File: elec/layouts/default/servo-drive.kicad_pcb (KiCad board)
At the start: 4 copper layers, 37.6 x 39.9 mm, 136 parts, among them U37 8Mhz

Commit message: Something fishy is going on with interfaces
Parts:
- removed U30: , lib:LED0603-RD
- added R40: , Resistor_SMD:R_0402_1005Metric, F.Cu at (179.8, 92.0)
- J1, R19, R20, U13, U2, U37: moved to B.Cu
- R39: value 1k -> (none)
- U26, U27: moved to F.Cu
- moved U2 66.5 mm to (222.4, 113.4), turned to 180 degrees
- moved J1 51.2 mm to (210.9, 115.7), turned to 180 degrees
- moved U25 50.9 mm to (229.0, 113.8), turned to -90 degrees
- moved U15 46.8 mm to (211.0, 118.7)
- moved R20 26.5 mm to (209.2, 111.4)
- moved R39 25.8 mm to (213.8, 92.7), turned to 180 degrees
- moved R24 25.0 mm to (213.9, 88.4), turned to 180 degrees
- moved U29 22.9 mm to (213.3, 89.6)
- moved R19 20.3 mm to (212.2, 111.3)
- moved U13 19.8 mm to (213.6, 89.9), turned to 45 degrees
- moved C1 19.8 mm to (197.6, 99.1)
- moved C19 19.8 mm to (197.6, 98.1)
- moved U37 17.4 mm to (208.9, 84.7), turned to -135 degrees
- moved U38 10.1 mm to (217.5, 114.4), turned to -90 degrees
- moved U23 9.04 mm to (222.3, 113.3)
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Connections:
- net SpinServoNEMA17-data_out renamed SpinServoNEMA17-data_in
- net SpinServoNEMA17-phase_b renamed SpinServoNEMA17-INLB
- net SpinServoNEMA17-phase_c renamed SpinServoNEMA17-INLC
- net _a-i_in-1 renamed _a-i_in-2
- net _b-i_in-1 renamed _b-i_in-2
- net _c-i_in-1 renamed _c-i_in-2
- net _i_sense-in-4 renamed _i_sense-gnd-7
- net _i_sense-in_n-6 renamed _i_sense-in_n
- net _i_sense-in_n-7 renamed _i_sense-in_n-1
- net _i_sense-in_n-8 renamed _i_sense-output-17
- net _i_sense-in_p-1 renamed _i_sense-output-15
- net _i_sense-in_p-2 renamed _i_sense-output-16
- net _i_sense-input-9 renamed _i_sense-p1-4
- net _i_sense-out-3 renamed _i_sense-in
- net _i_sense-out-4 renamed _i_sense-gnd-6
- net _i_sense-output-7 renamed _i_sense-output-14
- net ldo_3v3-adj-1 renamed ldo_3v3-adj
- net ldo_5v-output renamed ldo_5v-adj-1
- net micro-input-2 renamed micro-PF1_OSC_OUT-1
- C1 pad 1: SpinServoNEMA17-vcc -> SpinServoNEMA17-input
- C13 pad 1: SpinServoNEMA17-vcc -> SpinServoNEMA17-input
- C14 pad 1: SpinServoNEMA17-vcc -> SpinServoNEMA17-input
- C15 pad 1: SpinServoNEMA17-vcc -> SpinServoNEMA17-input
- C17 pad 1: SpinServoNEMA17-vcc -> SpinServoNEMA17-input
- C19 pad 1: SpinServoNEMA17-vcc -> SpinServoNEMA17-input
- C28 pad 1: SpinServoNEMA17-vcc-1 -> SpinServoNEMA17-in
- C40 pad 1: SpinServoNEMA17-vcc -> SpinServoNEMA17-input
- C41 pad 1: power_stage-bs-4 -> power_stage-bs-3
- C42 pad 1: micro-PF0_OSC_IN -> micro-in-1
- C43 pad 1: power_stage-bs-3 -> power_stage-bs-2
- C45 pad 1: power_stage-bs-2 -> power_stage-bs-1
- C46 pad 1: SpinServoNEMA17-vcc -> SpinServoNEMA17-gnd
- C46 pad 2: SpinServoNEMA17-gnd -> SpinServoNEMA17-input
- C7 pad 1: canbus-v_3_3-2 -> SpinServoNEMA17-input
- C7 pad 2: canbus-gnd-2 -> SpinServoNEMA17-gnd
- C9 pad 2: canbus-gnd-2 -> SpinServoNEMA17-gnd
- J1 pad 1: SpinServoNEMA17-gnd -> usbc-gnd
- J1 pad 2: SpinServoNEMA17-gnd -> usbc-gnd
- J1 pad 3: SpinServoNEMA17-gnd -> usbc-gnd
- J1 pad 4: SpinServoNEMA17-gnd -> usbc-gnd
- J1 pad A1: SpinServoNEMA17-gnd -> usbc-gnd
- J1 pad A12: SpinServoNEMA17-gnd -> usbc-gnd
- J1 pad A7: SpinServoNEMA17-gnd -> SpinServoNEMA17-dm
- J1 pad B1: SpinServoNEMA17-gnd -> usbc-gnd
- J1 pad B12: SpinServoNEMA17-gnd -> usbc-gnd
- J1 pad B7: SpinServoNEMA17-gnd -> SpinServoNEMA17-dm
- R1 pad 1: SpinServoNEMA17-vcc -> SpinServoNEMA17-input
- R10 pad 1: SpinServoNEMA17-dp -> micro-PA11-1
- R10 pad 2: SpinServoNEMA17-dp -> SpinServoNEMA17-dm
- R11 pad 1: SpinServoNEMA17-gnd -> micro-PA12-1
- R11 pad 2: SpinServoNEMA17-vcc -> SpinServoNEMA17-input
- R15 pad 1: SpinServoNEMA17-p3 -> SpinServoNEMA17-p2
- R2 pad 1: SpinServoNEMA17-vcc -> SpinServoNEMA17-input
- R21 pad 1: SpinServoNEMA17-vcc -> SpinServoNEMA17-input
- R23 pad 1: SpinServoNEMA17-p2 -> SpinServoNEMA17-p3
- R27 pad 1: SpinServoNEMA17-vcc-1 -> SpinServoNEMA17-in
- R3 pad 2: SpinServoNEMA17-in -> SpinServoNEMA17-in-1
- R39 pad 1: debug_led_2-A-2 -> SpinServoNEMA17-sda
- R39 pad 2: SpinServoNEMA17-gnd -> SpinServoNEMA17-input
- R9 pad 1: SpinServoNEMA17-gnd -> micro-PA12-1
- R9 pad 2: SpinServoNEMA17-gnd -> SpinServoNEMA17-dp
- U11 pad 1: SpinServoNEMA17-in -> SpinServoNEMA17-in-1
- U11 pad 2: SpinServoNEMA17-vcc -> SpinServoNEMA17-input
- U12 pad 14: power_stage-bs-2 -> power_stage-bs-1
- U12 pad 17: power_stage-bs-3 -> power_stage-bs-2
- U12 pad 20: power_stage-bs-4 -> power_stage-bs-3
- U12 pad 5: SpinServoNEMA17-vcc -> SpinServoNEMA17-input
- U13 pad 13: SpinServoNEMA17-in -> SpinServoNEMA17-in-1
- U13 pad 15: micro-PA7-2 -> SpinServoNEMA17-led_pixel
- U13 pad 20: SpinServoNEMA17-vcc -> SpinServoNEMA17-input
- U13 pad 21: SpinServoNEMA17-vcc -> SpinServoNEMA17-input
- U13 pad 22: micro-PB10-2 -> micro-tdo
- U13 pad 23: SpinServoNEMA17-vcc -> SpinServoNEMA17-input
- U13 pad 24: micro-PB11-2 -> SpinServoNEMA17-cs
- U13 pad 25: SpinServoNEMA17-cs -> SpinServoNEMA17-vin_sense
- U13 pad 30: SpinServoNEMA17-vin_sense -> micro-PA8-2
- U13 pad 33: SpinServoNEMA17-dp -> micro-PA11-1
- U13 pad 34: SpinServoNEMA17-gnd -> micro-PA12-1
- U13 pad 35: SpinServoNEMA17-vcc -> SpinServoNEMA17-input
- U13 pad 36: micro-tms -> micro-tms-1
- U13 pad 37: micro-tck-1 -> micro-tck-2
- U13 pad 38: micro-PA15 -> micro-tdi-1
- U13 pad 41: micro-PB3 -> micro-PB3-2
- U13 pad 42: micro-rst -> micro-PB4-1
- U13 pad 43: SpinServoNEMA17-led_pixel -> micro-PB5-1
- U13 pad 44: micro-PB6-2 -> micro-PB6-1
- U13 pad 46: SpinServoNEMA17-sda -> SpinServoNEMA17-scl
- U13 pad 47: SpinServoNEMA17-gnd -> SpinServoNEMA17-sda
- U13 pad 48: SpinServoNEMA17-vcc -> SpinServoNEMA17-input
- U13 pad 5: micro-PF0_OSC_IN -> micro-in-1
- U14 pad 2: SpinServoNEMA17-vcc-1 -> SpinServoNEMA17-in
- U15 pad 2: SpinServoNEMA17-vcc -> SpinServoNEMA17-input
- U15 pad 4: SpinServoNEMA17-gnd -> SpinServoNEMA17-scl
- U16 pad 1: SpinServoNEMA17-vcc -> SpinServoNEMA17-input
- U16 pad 10: micro-rst -> micro-tdo
- U16 pad 2: micro-tms -> micro-tck-2
- U16 pad 4: micro-tck-1 -> micro-vcc
- U16 pad 6: micro-PB3 -> micro-tdi-1
- U16 pad 8: micro-PA15 -> micro-tms-1
- U18 pad 10: SpinServoNEMA17-gnd -> SpinServoNEMA17-input
- U18 pad 13: SpinServoNEMA17-vcc -> SpinServoNEMA17-gnd
- U18 pad 17: SpinServoNEMA17-gnd -> SpinServoNEMA17-input
- U18 pad 8: SpinServoNEMA17-gnd -> SpinServoNEMA17-input
- U2 pad 1: xt30_2-gnd-1 -> SpinServoNEMA17-gnd
- U2 pad 2: xt30_2-vin-1 -> SpinServoNEMA17-in
- U20 pad 5: SpinServoNEMA17-vcc -> SpinServoNEMA17-input
- U21 pad 5: SpinServoNEMA17-vcc -> SpinServoNEMA17-input
- U23 pad 5: SpinServoNEMA17-vcc -> SpinServoNEMA17-input
- U24 pad 5: SpinServoNEMA17-vcc -> SpinServoNEMA17-input
- U25 pad 1: SpinServoNEMA17-gnd -> micro-PB6-1
- U25 pad 2: canbus-gnd-2 -> SpinServoNEMA17-gnd
- U25 pad 3: canbus-v_3_3-2 -> SpinServoNEMA17-input
- U25 pad 4: SpinServoNEMA17-dp -> micro-PB5-1
- U25 pad 6: SpinServoNEMA17-p2 -> SpinServoNEMA17-p3
- U25 pad 7: SpinServoNEMA17-p3 -> SpinServoNEMA17-p2
- U25 pad 8: canbus-gnd-2 -> SpinServoNEMA17-gnd
- U26 pad 1: SpinServoNEMA17-gnd -> SpinServoNEMA17-input
- U27 pad 1: SpinServoNEMA17-gnd -> SpinServoNEMA17-input
- U29 pad 1: micro-PF0_OSC_IN -> micro-PB4-1
- U37 pad 1: micro-PF0_OSC_IN -> micro-in-1
- U4 pad 5: SpinServoNEMA17-vcc -> SpinServoNEMA17-input
- U6 pad 4: SpinServoNEMA17-vcc-1 -> SpinServoNEMA17-in
- U6 pad 5: SpinServoNEMA17-vcc-1 -> SpinServoNEMA17-in
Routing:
- net (no net): track 153.2 -> 54.9 mm, vias 12 -> 2
- net SpinServoNEMA17-p2: track 0.00 -> 28.0 mm, vias 0 -> 4
- net SpinServoNEMA17-c_isense: track 27.3 -> 0.04 mm, vias 2 -> 0
- net SpinServoNEMA17-INLB: track 32.6 -> 6.98 mm, vias 4 -> 3
- net SpinServoNEMA17-in: track 17.5 -> 0.00 mm, vias 2 -> 0
- net SpinServoNEMA17-phase_a: track 34.3 -> 17.3 mm, vias 4 -> 3
- net SpinServoNEMA17-a_isense: track 17.7 -> 1.12 mm, vias 2 -> 1
- net SpinServoNEMA17-in-1: track 0.00 -> 16.2 mm, vias 0 -> 1
- net micro-tdi-1: track 0.00 -> 15.0 mm, vias 0 -> 2
- net micro-tck-1: track 11.8 -> 0.00 mm, vias 1 -> 0
- net micro-tms-1: track 0.00 -> 10.3 mm, vias 0 -> 1
- net micro-tms: track 10.3 -> 0.00 mm, vias 1 -> 0
- net micro-PB3: track 9.85 -> 0.00 mm, vias 1 -> 0
- net SpinServoNEMA17-vcc: track 8.80 -> 0.00 mm, vias 6 -> 0
- net SpinServoNEMA17-data_in: track 7.35 -> 0.00 mm
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- removed copper zone on F.Cu, net SpinServoNEMA17-vcc-1
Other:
- board text removed: "BOOT0"
- board text removed: "RESET"

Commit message: layout complete
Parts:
- removed U38: , lib:SOD-323_L1.8-W1.3-LS2.5-RD
- added U30: , lib:SOD-323_L1.8-W1.3-LS2.5-RD, F.Cu at (217.6, 114.3)
- C13, C14, C15, C17, C40, C42, C44, R10, R11, R7, R9: moved to B.Cu
- moved R15 55.4 mm to (237.2, 113.7)
- moved R23 55.0 mm to (237.2, 114.7)
- moved C9 53.4 mm to (237.2, 112.8), turned to 180 degrees
- moved R40 41.9 mm to (213.6, 116.7), turned to -90 degrees
- moved C17 40.5 mm to (219.0, 86.7), turned to 45 degrees
- moved C14 40.4 mm to (214.4, 96.5), turned to -45 degrees
- moved C13 40.0 mm to (217.6, 85.2), turned to 45 degrees
- moved C15 39.8 mm to (215.1, 95.8), turned to -45 degrees
- moved C40 39.6 mm to (218.3, 85.9), turned to 45 degrees
- moved R9 35.7 mm to (210.1, 111.3), turned to -90 degrees
- moved R10 34.6 mm to (211.2, 111.3), turned to -90 degrees
- moved C44 31.9 mm to (210.5, 83.2), turned to 135 degrees
- moved R11 28.1 mm to (216.8, 95.4), turned to -90 degrees
- moved C42 28.0 mm to (206.8, 83.5), turned to 45 degrees
- moved C7 27.2 mm to (210.7, 108.0), turned to 90 degrees
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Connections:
- net SpinServoNEMA17-INLB renamed SpinServoNEMA17-INHB
- net SpinServoNEMA17-INLC renamed SpinServoNEMA17-INHC
- net SpinServoNEMA17-phase_a renamed SpinServoNEMA17-PA0
- net SpinServoNEMA17-vbus renamed usbc-vbus-1
- net SpinServoNEMA17-vin_sense renamed SpinServoNEMA17-out-1
- net _a-i_in-2 renamed _a-gnd
- net _b-i_in-2 renamed _b-i_in-1
- net _c-i_in-2 renamed _c-i_in
- net _i_sense-gnd-6 renamed _i_sense-gnd
- net _i_sense-gnd-7 renamed _i_sense-out-1
- net _i_sense-in renamed _i_sense-in-6
- net _i_sense-in_n renamed _i_sense-in_n-7
- net _i_sense-in_n-1 renamed _i_sense-output-6
- net _i_sense-input-14 renamed _i_sense-p1-6
- net _i_sense-output-14 renamed _i_sense-output-4
- net _i_sense-output-15 renamed _i_sense-output-5
- net _i_sense-output-16 renamed _i_sense-output-7
- net _i_sense-output-17 renamed _i_sense-in_n-8
- net micro-PB5-1 renamed micro-can_rx
- net micro-PB6-1 renamed micro-can_tx
- net micro-in-1 renamed micro-PF0_OSC_IN
- C1 pad 1: SpinServoNEMA17-input -> SpinServoNEMA17-out
- C13 pad 1: SpinServoNEMA17-input -> SpinServoNEMA17-out
- C14 pad 1: SpinServoNEMA17-input -> SpinServoNEMA17-out
- C15 pad 1: SpinServoNEMA17-input -> SpinServoNEMA17-out
- C16 pad 1: SpinServoNEMA17-gnd -> SpinServoNEMA17-vcc
- C17 pad 1: SpinServoNEMA17-input -> SpinServoNEMA17-out
- C18 pad 1: SpinServoNEMA17-gnd -> SpinServoNEMA17-vcc
- C19 pad 1: SpinServoNEMA17-input -> SpinServoNEMA17-out
- C20 pad 1: power_stage-vcc_pwr-1 -> SpinServoNEMA17-in
- C21 pad 1: power_stage-vcc_pwr-1 -> SpinServoNEMA17-in
- C22 pad 1: power_stage-vcc_pwr-1 -> SpinServoNEMA17-in
- C23 pad 1: SpinServoNEMA17-gnd -> SpinServoNEMA17-vin
- C25 pad 1: power_stage-vcc_pwr-1 -> SpinServoNEMA17-in
- C26 pad 1: power_stage-vcc_pwr-1 -> SpinServoNEMA17-in
- C27 pad 1: power_stage-vcc_pwr-1 -> SpinServoNEMA17-in
- C29 pad 1: power_stage-vcc_pwr-1 -> SpinServoNEMA17-in
- C3 pad 1: power_stage-vcc_pwr-1 -> SpinServoNEMA17-in
- C30 pad 1: power_stage-vcc_pwr-1 -> SpinServoNEMA17-in
- C31 pad 1: SpinServoNEMA17-gnd -> SpinServoNEMA17-vin
- C32 pad 1: SpinServoNEMA17-gnd -> SpinServoNEMA17-vin
- C35 pad 1: power_stage-vcc_pwr-1 -> SpinServoNEMA17-in
- C36 pad 1: power_stage-vcc_pwr-1 -> SpinServoNEMA17-in
- C37 pad 1: power_stage-vcc_pwr-1 -> SpinServoNEMA17-in
- C38 pad 1: power_stage-vcc_pwr-1 -> SpinServoNEMA17-in
- C39 pad 1: power_stage-vcc_pwr-1 -> SpinServoNEMA17-in
- C4 pad 1: power_stage-vcc_pwr-1 -> SpinServoNEMA17-in
- C40 pad 1: SpinServoNEMA17-input -> SpinServoNEMA17-out
- C41 pad 1: power_stage-bs-3 -> power_stage-BSTA-1
- C43 pad 1: power_stage-bs-2 -> power_stage-bs-3
- C45 pad 1: power_stage-bs-1 -> power_stage-bs-2
- C46 pad 1: SpinServoNEMA17-gnd -> SpinServoNEMA17-out
- C46 pad 2: SpinServoNEMA17-input -> SpinServoNEMA17-gnd
- C47 pad 1: power_stage-vcc_pwr-1 -> SpinServoNEMA17-in
- C48 pad 1: power_stage-vcc_pwr-1 -> SpinServoNEMA17-in
- C49 pad 1: power_stage-vcc_pwr-1 -> SpinServoNEMA17-in
- C5 pad 1: SpinServoNEMA17-gnd -> SpinServoNEMA17-vin
- C6 pad 1: power_stage-vcc_pwr-1 -> SpinServoNEMA17-in
- C7 pad 1: SpinServoNEMA17-input -> SpinServoNEMA17-out
- C8 pad 1: SpinServoNEMA17-gnd -> SpinServoNEMA17-vin
- J1 pad 1: usbc-gnd -> SpinServoNEMA17-gnd
- J1 pad 2: usbc-gnd -> SpinServoNEMA17-gnd
- J1 pad 3: usbc-gnd -> SpinServoNEMA17-gnd
- J1 pad 4: usbc-gnd -> SpinServoNEMA17-gnd
- J1 pad A1: usbc-gnd -> SpinServoNEMA17-gnd
- J1 pad A12: usbc-gnd -> SpinServoNEMA17-gnd
- J1 pad B1: usbc-gnd -> SpinServoNEMA17-gnd
- J1 pad B12: usbc-gnd -> SpinServoNEMA17-gnd
- R1 pad 1: SpinServoNEMA17-input -> SpinServoNEMA17-out
- R11 pad 2: SpinServoNEMA17-input -> SpinServoNEMA17-out
- R13 pad 1: _i_sense-p1-4 -> _i_sense-input-10
- R17 pad 1: SpinServoNEMA17-gnd -> SpinServoNEMA17-vcc
- R2 pad 1: SpinServoNEMA17-input -> SpinServoNEMA17-out
- R21 pad 1: SpinServoNEMA17-input -> SpinServoNEMA17-out
- R25 pad 1: _i_sense-input-12 -> _i_sense-p1-5
- R29 pad 1: SpinServoNEMA17-gnd -> SpinServoNEMA17-vin
- R39 pad 2: SpinServoNEMA17-input -> SpinServoNEMA17-out
- R40 pad 2: SpinServoNEMA17-input -> SpinServoNEMA17-out
- R50 pad 1: _i_sense-input-13 -> _i_sense-input-12
- R6 pad 1: _i_sense-input-10 -> _i_sense-p1-4
- U1 pad 10: _hb-vcc_pwr-8 -> SpinServoNEMA17-in
- U1 pad 2: _hb-vcc_pwr-8 -> SpinServoNEMA17-in
- U1 pad 3: _hb-vcc_pwr-8 -> SpinServoNEMA17-in
- U1 pad 4: _hb-vcc_pwr-8 -> SpinServoNEMA17-in
- U10 pad 2: SpinServoNEMA17-gnd -> SpinServoNEMA17-vin
- U11 pad 2: SpinServoNEMA17-input -> SpinServoNEMA17-out
- U12 pad 14: power_stage-bs-1 -> power_stage-bs-2
- U12 pad 17: power_stage-bs-2 -> power_stage-bs-3
- U12 pad 20: power_stage-bs-3 -> power_stage-BSTA-1
- U12 pad 4: SpinServoNEMA17-gnd -> SpinServoNEMA17-vin
- U12 pad 5: SpinServoNEMA17-input -> SpinServoNEMA17-out
- U13 pad 15: SpinServoNEMA17-led_pixel -> SpinServoNEMA17-data_in
- U13 pad 20: SpinServoNEMA17-input -> SpinServoNEMA17-out
- U13 pad 21: SpinServoNEMA17-input -> SpinServoNEMA17-out
- U13 pad 22: micro-tdo -> micro-PB10-2
- U13 pad 23: SpinServoNEMA17-input -> SpinServoNEMA17-out
- U13 pad 35: SpinServoNEMA17-input -> SpinServoNEMA17-out
- U13 pad 37: micro-tck-2 -> micro-tck-1
- U13 pad 41: micro-PB3-2 -> micro-tdo
- U13 pad 42: micro-PB4-1 -> micro-reset
- U13 pad 48: SpinServoNEMA17-input -> SpinServoNEMA17-out
- U15 pad 2: SpinServoNEMA17-input -> SpinServoNEMA17-out
- U16 pad 1: SpinServoNEMA17-input -> SpinServoNEMA17-out
- U16 pad 10: micro-tdo -> micro-reset
- U16 pad 2: micro-tck-2 -> micro-tms-1
- U16 pad 4: micro-vcc -> micro-tck-1
- U16 pad 6: micro-tdi-1 -> micro-tdo
- U16 pad 8: micro-tms-1 -> micro-tdi-1
- U17 pad 1: _i_sense-p1-4 -> _i_sense-input-10
- U18 pad 10: SpinServoNEMA17-input -> SpinServoNEMA17-gnd
- U18 pad 13: SpinServoNEMA17-gnd -> SpinServoNEMA17-out
- U18 pad 17: SpinServoNEMA17-input -> SpinServoNEMA17-gnd
- U18 pad 8: SpinServoNEMA17-input -> SpinServoNEMA17-gnd
- U19 pad 1: _i_sense-input-10 -> _i_sense-p1-4
- U20 pad 5: SpinServoNEMA17-input -> SpinServoNEMA17-out
- U21 pad 5: SpinServoNEMA17-input -> SpinServoNEMA17-out
- U22 pad 1: SpinServoNEMA17-gnd -> SpinServoNEMA17-vin
- U22 pad 3: SpinServoNEMA17-gnd -> SpinServoNEMA17-vin
- U22 pad 5: SpinServoNEMA17-gnd -> SpinServoNEMA17-vcc
- U23 pad 1: SpinServoNEMA17-gnd -> SpinServoNEMA17-vcc
- U23 pad 3: SpinServoNEMA17-gnd -> SpinServoNEMA17-vcc
- U23 pad 5: SpinServoNEMA17-input -> SpinServoNEMA17-out
- U24 pad 5: SpinServoNEMA17-input -> SpinServoNEMA17-out
- U25 pad 3: SpinServoNEMA17-input -> SpinServoNEMA17-out
- U26 pad 1: SpinServoNEMA17-input -> SpinServoNEMA17-vcc
- U27 pad 1: SpinServoNEMA17-input -> SpinServoNEMA17-vcc
- U27 pad 2: SpinServoNEMA17-p3 -> SpinServoNEMA17-p2
- U27 pad 3: SpinServoNEMA17-p2 -> SpinServoNEMA17-p3
- U28 pad 10: _hb-vcc_pwr-7 -> SpinServoNEMA17-in
- U28 pad 2: _hb-vcc_pwr-7 -> SpinServoNEMA17-in
- U28 pad 3: _hb-vcc_pwr-7 -> SpinServoNEMA17-in
- U28 pad 4: _hb-vcc_pwr-7 -> SpinServoNEMA17-in
- U29 pad 1: micro-PB4-1 -> micro-reset
- U3 pad 10: _hb-vcc_pwr-9 -> SpinServoNEMA17-in
- U3 pad 2: _hb-vcc_pwr-9 -> SpinServoNEMA17-in
- U3 pad 3: _hb-vcc_pwr-9 -> SpinServoNEMA17-in
- U3 pad 4: _hb-vcc_pwr-9 -> SpinServoNEMA17-in
- U32 pad 1: SpinServoNEMA17-gnd -> SpinServoNEMA17-vcc
- U32 pad 4: SpinServoNEMA17-data_in -> SpinServoNEMA17-data_out
- U33 pad 1: _i_sense-input-12 -> _i_sense-p1-5
- U34 pad 1: _i_sense-input-13 -> _i_sense-input-12
- U4 pad 5: SpinServoNEMA17-input -> SpinServoNEMA17-out
- U5 pad 1: SpinServoNEMA17-gnd -> SpinServoNEMA17-vcc
- U5 pad 3: SpinServoNEMA17-data_in -> SpinServoNEMA17-data_out
- U5 pad 4: SpinServoNEMA17-led_pixel -> SpinServoNEMA17-data_in
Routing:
- net SpinServoNEMA17-out: track 0.00 -> 113.7 mm, vias 0 -> 12
- net SpinServoNEMA17-vcc: track 0.00 -> 71.8 mm, vias 0 -> 4
- net (no net): track 54.9 -> 0.00 mm, vias 2 -> 0
- net micro-can_rx: track 0.00 -> 37.4 mm, vias 0 -> 2
- net SpinServoNEMA17-vin: track 0.00 -> 37.1 mm
- net micro-can_tx: track 0.00 -> 35.9 mm, vias 0 -> 2
- net SpinServoNEMA17-scl: track 0.00 -> 31.0 mm, vias 0 -> 2
- net SpinServoNEMA17-sda: track 1.44 -> 30.1 mm, vias 0 -> 2
- net SpinServoNEMA17-p3: track 0.00 -> 28.3 mm
- net SpinServoNEMA17-c_isense: track 0.04 -> 24.6 mm, vias 0 -> 2
- net power_stage-i_fb_zero-1: track 23.7 -> 48.2 mm, vias 2 -> 4
- net SpinServoNEMA17-INHB: track 6.98 -> 30.2 mm
- net SpinServoNEMA17-gnd: track 20.0 -> 43.0 mm, vias 170 -> 96
- net SpinServoNEMA17-temp_sense: track 1.10 -> 23.8 mm, vias 0 -> 2
- net micro-PA12-1: track 0.00 -> 21.2 mm, vias 0 -> 2
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- added copper zone on B.Cu, net SpinServoNEMA17-in
- added copper zone on F.Cu, net SpinServoNEMA17-in
- added copper zone on In1.Cu, net SpinServoNEMA17-in
- added copper zone on In2.Cu, net SpinServoNEMA17-in
- added copper zone on In2.Cu, net SpinServoNEMA17-out
- removed copper zone on In2.Cu, net ldo_3v3-adj
- removed copper zone on B.Cu, net power_stage-vcc_pwr-1
- removed copper zone on F.Cu, net power_stage-vcc_pwr-1
- removed copper zone on In2.Cu, net power_stage-vcc_pwr-1

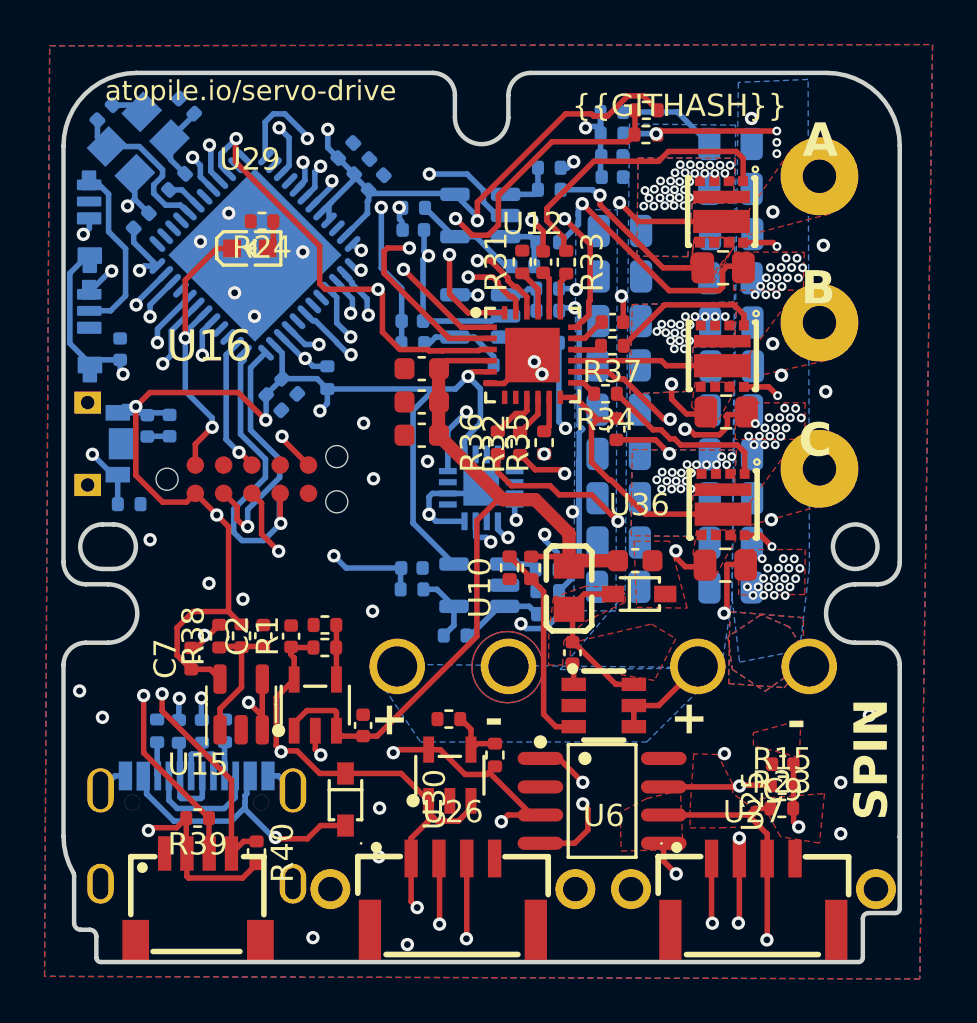
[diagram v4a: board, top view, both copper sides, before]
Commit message: fixed githash location, cleaned up silkscreen
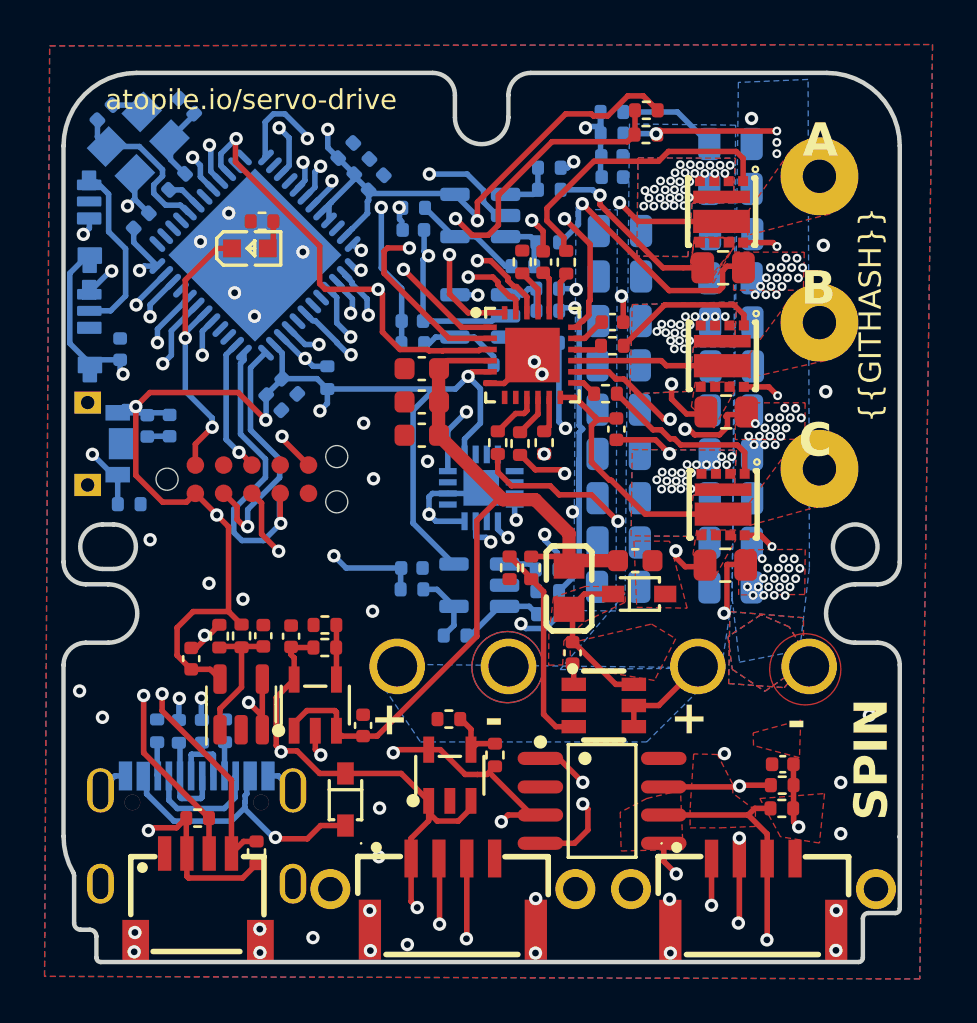
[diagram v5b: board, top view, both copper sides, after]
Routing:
- net SpinServoNEMA17-vcc: track 71.8 -> 70.9 mm
- net SpinServoNEMA17-gnd: vias 96 -> 104

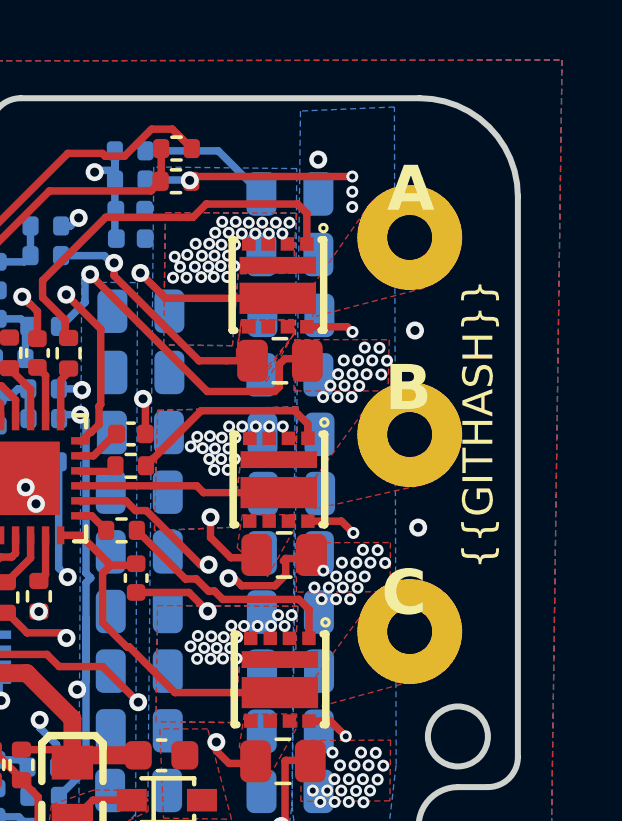
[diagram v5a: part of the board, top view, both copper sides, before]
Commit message: Minor silk fixes
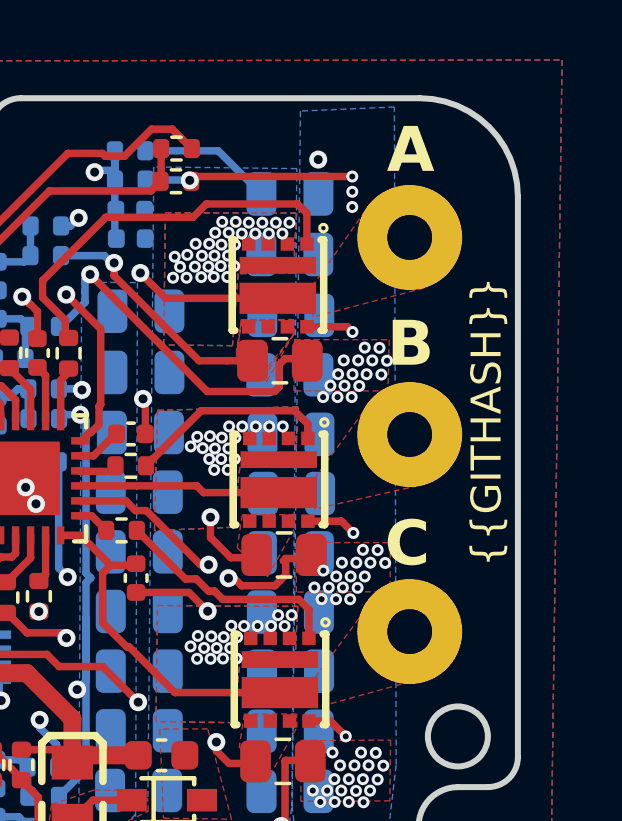
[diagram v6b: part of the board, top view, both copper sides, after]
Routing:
- net SpinServoNEMA17-gnd: vias 104 -> 102
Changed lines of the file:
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@@
     (effects (font (size 1.5 1.5) (thickness 0.3) bold) (justify left bottom))
   )
-  (gr_text "{{GITHASH}} " (at 241.772523 97.421219 90) (layer "F.SilkS")
+  (gr_text "{{GITHASH}} " (at 242.047256 97.338502 90) (layer "F.SilkS")
     (effects (font (size 1 1) (thickness 0.1)) (justify left bottom))
   )
@@
     (effects (font (size 1.5 1.5) (thickness 0.3) bold) (justify left bottom))
   )
-  (gr_text "C" (at 237.951688 99.086505) (layer "F.SilkS")
+  (gr_text "C" (at 238.061717 97.442768) (layer "F.SilkS")
     (effects (font (size 1.5 1.5) (thickness 0.3) bold) (justify left bottom))
   )
-  (gr_text "B" (at 238.064227 92.259142) (layer "F.SilkS")
+  (gr_text "B" (at 238.141749 90.786496) (layer "F.SilkS")
     (effects (font (size 1.5 1.5) (thickness 0.3) bold) (justify left bottom))
   )
-  (gr_text "A" (at 238.139253 85.619344) (layer "F.SilkS")
+  (gr_text "A" (at 238.132257 84.324109) (layer "F.SilkS")
     (effects (font (size 1.5 1.5) (thickness 0.3) bold) (justify left bottom))
   )
@@
   (via (at 236.910788 98.417901) (size 0.4) (drill 0.2) (layers "F.Cu" "B.Cu") (free) (net 5))
   (via (at 212.636139 91.591871) (size 0.6) (drill 0.3) (layers "F.Cu" "B.Cu") (net 5))
-  (via (at 239.072249 89.459824) (size 0.6) (drill 0.3) (layers "F.Cu" "B.Cu") (net 5))
   (via (at 236.395702 105.175383) (size 0.4) (drill 0.2) (layers "F.Cu" "B.Cu") (free) (net 5))
   (via (at 236.990124 90.917644) (size 0.4) (drill 0.2) (layers "F.Cu" "B.Cu") (free) (net 5))
@@
   (via (at 216.151723 120.545237) (size 0.6) (drill 0.3) (layers "F.Cu" "B.Cu") (net 5))
   (via (at 218.70333 119.331418) (size 0.6) (drill 0.3) (layers "F.Cu" "B.Cu") (free) (net 5))
-  (via (at 239.178801 96.030482) (size 0.6) (drill 0.3) (layers "F.Cu" "B.Cu") (net 5))
   (via (at 218.830167 105.889286) (size 0.6) (drill 0.3) (layers "F.Cu" "B.Cu") (net 5))
   (via (at 226.095193 94.690527) (size 0.6) (drill 0.3) (layers "F.Cu" "B.Cu") (net 5))
